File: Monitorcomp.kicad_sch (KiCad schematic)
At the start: 5 parts, among them Q1 2N2219, U2 LM393

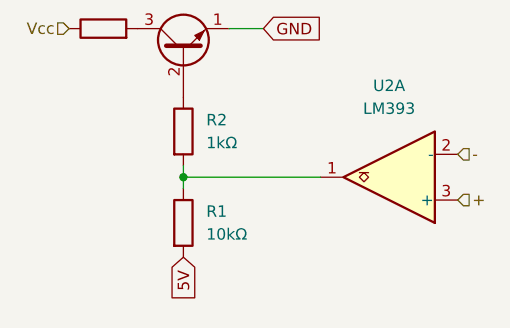
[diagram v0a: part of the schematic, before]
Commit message: DC-DC converter setup
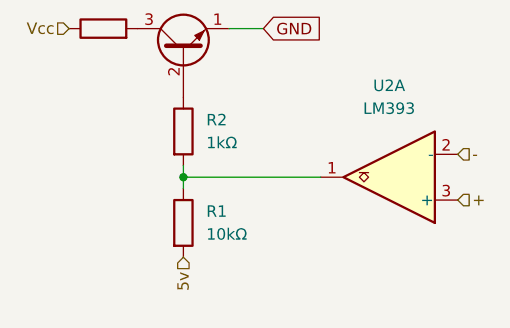
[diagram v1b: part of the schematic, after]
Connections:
- net 5V renamed 5v
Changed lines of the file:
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@@
-		)
-	)
-	(global_label "5V"
-		(shape input)
-		(at 151.13 97.79 270)
-		(fields_autoplaced yes)
-		(effects
-			(font
-				(size 1.27 1.27)
-			)
-			(justify right)
-		)
-		(property "Intersheetrefs" "${INTERSHEET_REFS}"
-			(at 151.13 102.4191 90)
-			(effects
-				(font
-					(size 1.27 1.27)
-				)
-				(justify right)
-				(hide yes)
-			)
 		)
 	)
@@
 		)
 	)
+	(hierarchical_label "5v"
+		(shape input)
+		(at 151.13 97.79 270)
+		(fields_autoplaced yes)
+		(effects
+			(font
+				(size 1.27 1.27)
+			)
+			(justify right)
+		)
+	)

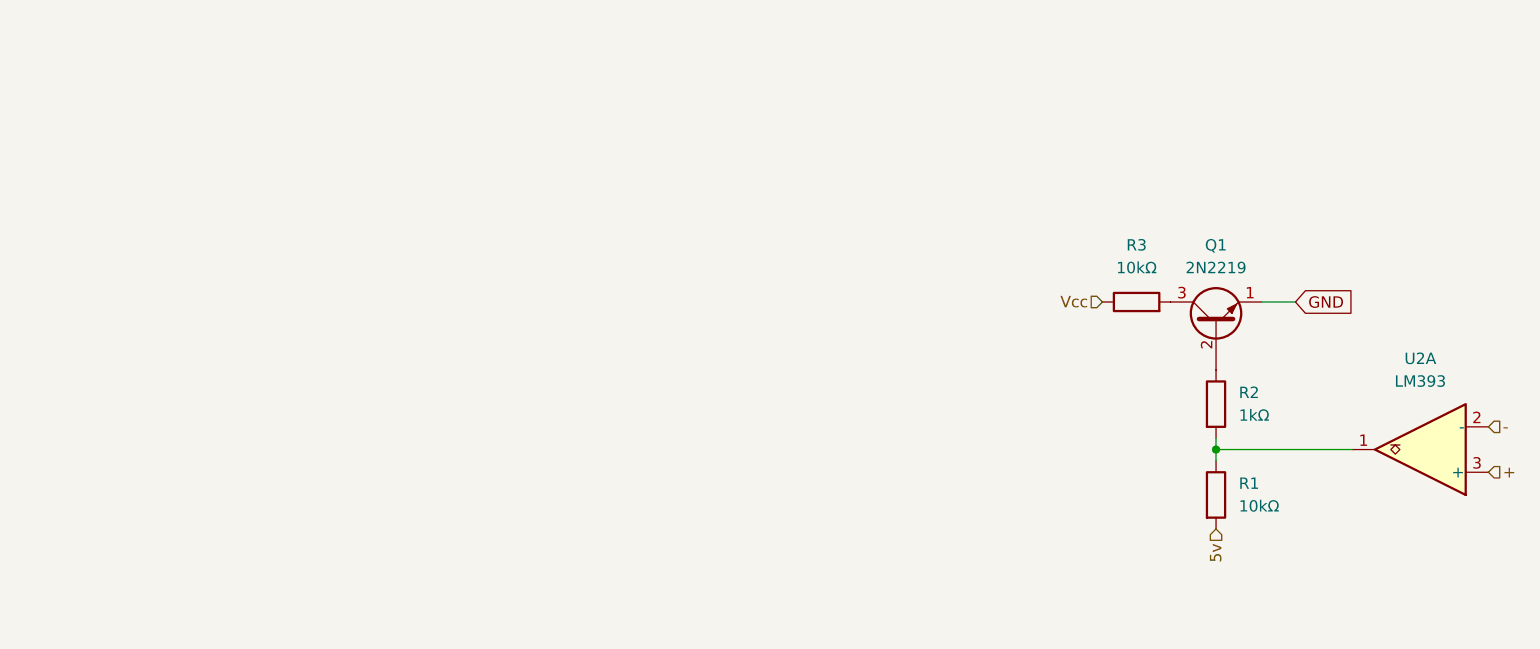
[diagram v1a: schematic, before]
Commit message: POR implementation
added POR and fixed amplifier
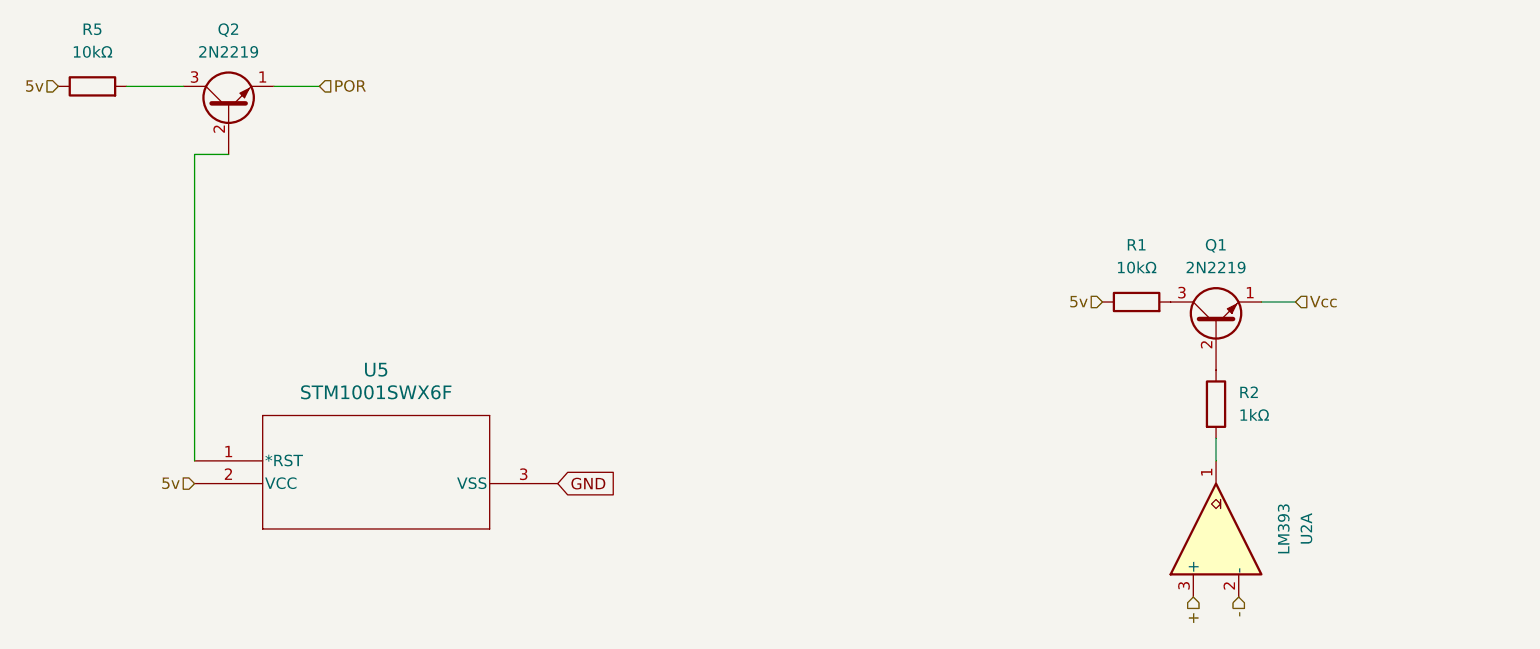
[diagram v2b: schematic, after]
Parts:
- removed R3: 10kΩ, Resistor_THT:R_Axial_DIN0204_L3.6mm_D1.6mm_P5.08mm_Horizontal, symbol Device:R
- added Q2: 2N2219, Package_TO_SOT_THT:TO-39-3, symbol Transistor_BJT:2N2219
- added R5: 10kΩ, Resistor_THT:R_Axial_DIN0204_L3.6mm_D1.6mm_P5.08mm_Horizontal, symbol Device:R
- added U5: STM1001SWX6F, SOT-23_STM, symbol POR:STM1001SWX6F
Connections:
- net 5v: now also R1.1, R5.1, U5.2 (VCC); no longer R1.2
- net GND: now also U5.3 (VSS); no longer Q1.1 (E)
- net Vcc: now also Q1.1 (E)
- net at R2.2, U2.1: no longer R1.1
- net at Q1.3 (C): now also R1.2
- new net: Q2.3 (C), R5.2
- new net: Q2.2 (B), U5.1 (*RST)
- new net POR: Q2.1 (E)
